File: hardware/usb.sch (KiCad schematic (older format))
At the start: 17 parts, among them J901 USB_OTG, U901 NX5P3090, U902 SMP1255PUTG, U903 USB3320, U904 OSC

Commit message: Length matched DDR3 Memory again.
Forgot to keep enough space between the traces and between the meander waves.

Also, I switched to Kicad 5.0 RC2.

Swaped a few ddr signals.
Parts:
- C901, C902, C903, C904, C905, C906, C907: symbol C -> device:C
- J901: symbol USB_OTG -> conn:USB_OTG
- R901, R902, R903, R904, R905: symbol R -> device:R
- U901: symbol NX5P3090 -> nx5p3090:NX5P3090
- U902: symbol SMP1255PUTG -> smp1255putg:SMP1255PUTG
- U903: symbol USB3320 -> usb3320:USB3320
- U904: symbol OSC -> osc:OSC
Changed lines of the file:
@@
-EESchema Schematic File Version 2
-LIBS:zynq_board-rescue
-LIBS:power
-LIBS:device
-LIBS:transistors
-LIBS:conn
-LIBS:linear
-LIBS:regul
-LIBS:74xx
-LIBS:cmos4000
-LIBS:adc-dac
-LIBS:memory
-LIBS:xilinx
-LIBS:microcontrollers
-LIBS:dsp
-LIBS:microchip
-LIBS:analog_switches
-LIBS:motorola
-LIBS:texas
-LIBS:intel
-LIBS:audio
-LIBS:interface
-LIBS:digital-audio
-LIBS:philips
-LIBS:display
-LIBS:cypress
-LIBS:siliconi
-LIBS:opto
-LIBS:atmel
-LIBS:contrib
-LIBS:valves
-LIBS:xilinx_zynq_clg485
-LIBS:SFP_plus
-LIBS:ael2005
-LIBS:diff_osc
-LIBS:si53340
-LIBS:usb3320
-LIBS:nx5p3090
-LIBS:smp1255putg
-LIBS:osc
-LIBS:ddr
-LIBS:misc
-LIBS:tlk10031
-LIBS:lshm-150-xxx-x-dv-a-s
-LIBS:sn74axc8t245
-LIBS:sn74lvc2t45
-LIBS:dmf05lcflp
-LIBS:bss138ps
-LIBS:max14854
-LIBS:switches
-LIBS:ft234xd
-LIBS:sn74lv1t126
-LIBS:emif06-msd02n16
-LIBS:cat24c02tdi-gt3
-LIBS:power_symbols
-LIBS:ti_power_modules
-LIBS:mdr20
-LIBS:dm3cs
-LIBS:lsf0102
-LIBS:dmp3056l
+EESchema Schematic File Version 4
 LIBS:zynq_board-cache
-EELAYER 25 0
+EELAYER 26 0
 EELAYER END
 $Descr A4 11693 8268
@@
 $EndDescr
 $Comp
-L USB3320 U903
+L usb3320:USB3320 U903
 U 1 1 59915033
 P 7100 3800
@@
 CLK
 $Comp
-L GND #PWR096
+L power1:GND #PWR096
 U 1 1 59921269
 P 7100 5100
@@
 NoConn ~ 6100 4700
 $Comp
-L R R905
+L device:R R905
 U 1 1 59921EA9
 P 8250 4700
@@
 $EndComp
 $Comp
-L GND #PWR097
+L power1:GND #PWR097
 U 1 1 59921EDC
 P 8500 4800
@@
 	8500 4700 8500 4800
 $Comp
-L GND #PWR098
+L power1:GND #PWR098
 U 1 1 59921F43
 P 1200 4700
@@
 $EndComp
 $Comp
-L R R901
+L device:R R901
 U 1 1 59922379
 P 1000 4550
@@
 $EndComp
 $Comp
-L GND #PWR099
+L power1:GND #PWR099
 U 1 1 599223A7
 P 1000 4700
@@
 $EndComp
 $Comp
-L R R904
+L device:R R904
 U 1 1 599227D7
 P 5750 3600
@@
 $EndComp
 $Comp
-L C C901
+L device:C C901
 U 1 1 599228B6
 P 1850 4350
@@
 	1200 4200 1200 4700
 $Comp
-L GND #PWR0100
+L power1:GND #PWR0100
 U 1 1 599229B3
 P 1850 4700
@@
 	1850 4700 1850 4500
 $Comp
-L +1V8 #PWR0101
+L power1:+1V8 #PWR0101
 U 1 1 59922E8F
 P 6850 1600
@@
 $EndComp
 $Comp
-L C C904
+L device:C C904
 U 1 1 5992426F
 P 6850 1850
@@
 $EndComp
 $Comp
-L C C905
+L device:C C905
 U 1 1 59924337
 P 7350 1850
@@
 	6850 1600 6850 1700
 $Comp
-L +1V8 #PWR0102
+L power1:+1V8 #PWR0102
 U 1 1 599243A9
 P 7350 1600
@@
 	7350 1700 7350 1600
 $Comp
-L GND #PWR0103
+L power1:GND #PWR0103
 U 1 1 5992454D
 P 7350 2000
@@
 $EndComp
 $Comp
-L GND #PWR0104
+L power1:GND #PWR0104
 U 1 1 5992459D
 P 6850 2000
@@
 Connection ~ 6850 1650
 $Comp
-L C C903
+L device:C C903
 U 1 1 59924B0A
 P 6400 1850
@@
 	6850 1650 7100 1650
 $Comp
-L +3V3 #PWR0105
+L power1:+3V3 #PWR0105
 U 1 1 59924C11
 P 6400 1600
@@
 $EndComp
 $Comp
-L GND #PWR0106
+L power1:GND #PWR0106
 U 1 1 59924C37
 P 6400 2000
@@
 VBUS overvoltage protection resistor\nPower rating for 30V protection: 0.625W
 $Comp
-L NX5P3090 U901
+L nx5p3090:NX5P3090 U901
 U 1 1 5A971EC5
 P 3800 3200
@@
 $EndComp
 $Comp
-L SMP1255PUTG U902
+L smp1255putg:SMP1255PUTG U902
 U 1 1 5A98470D
 P 3800 4600
@@
 Connection ~ 4700 4700
 $Comp
-L GND #PWR0107
+L power1:GND #PWR0107
 U 1 1 5A984E78
 P 4700 4800
@@
 $EndComp
 $Comp
-L GND #PWR0108
+L power1:GND #PWR0108
 U 1 1 5A985319
 P 3100 3400
@@
 	5350 3500 6100 3500
 $Comp
-L C C902
+L device:C C902
 U 1 1 5A9853C5
 P 4700 2750
@@
 $EndComp
 $Comp
-L GND #PWR0109
+L power1:GND #PWR0109
 U 1 1 5A985418
 P 4700 2900
@@
 $EndComp
 $Comp
-L +5V #PWR0110
+L power1:+5V #PWR0110
 U 1 1 5A985450
 P 4700 2400
@@
 	4700 4600 4700 4800
 $Comp
-L R R902
+L device:R R902
 U 1 1 5A985A8D
 P 4650 3200
@@
 $EndComp
 $Comp
-L GND #PWR0111
+L power1:GND #PWR0111
 U 1 1 5A985AE5
 P 4800 3200
@@
 ILIM current limit adjustment resistor:\nR=100k for I_ocp=581 mA typ.
 $Comp
-L R R903
+L device:R R903
 U 1 1 5A986061
 P 5150 3100
@@
 Connection ~ 5150 3300
 $Comp
-L +1V8 #PWR0112
+L power1:+1V8 #PWR0112
 U 1 1 5A9861C7
 P 5150 2950
@@
 NoConn ~ 8100 4400
 $Comp
-L OSC U904
+L osc:OSC U904
 U 1 1 5A98852C
 P 9500 4050
@@
 	10100 4150 10000 4150
 $Comp
-L GND #PWR0113
+L power1:GND #PWR0113
 U 1 1 5A98862B
 P 8900 4250
@@
 	8900 4150 9000 4150
 $Comp
-L C C907
+L device:C C907
 U 1 1 5A98874B
 P 10350 4100
@@
 Connection ~ 10050 3800
 $Comp
-L +1V8 #PWR0114
+L power1:+1V8 #PWR0114
 U 1 1 5A9888CB
 P 10050 3700
@@
 $EndComp
 $Comp
-L GND #PWR0115
+L power1:GND #PWR0115
 U 1 1 5A988966
 P 10350 4250
@@
 $EndComp
 $Comp
-L GND #PWR0116
+L power1:GND #PWR0116
 U 1 1 5A988E5D
 P 6000 3300
@@
 	5900 2450 7650 2450
 $Comp
-L C C906
+L device:C C906
 U 1 1 5A9894AA
 P 7800 1850
@@
 	7800 1600 7800 1700
 $Comp
-L GND #PWR0117
+L power1:GND #PWR0117
 U 1 1 5A989692
 P 7800 2000
@@
 Oscillator: DSC6003CI2A-012.0000\n(12 MHz)
 $Comp
-L USB_OTG J901
+L conn:USB_OTG J901
 U 1 1 5ACE0B3C
 P 1200 3800
@@
 	1100 4300 1100 4200
 $Comp
-L +3V3 #PWR0118
+L power1:+3V3 #PWR0118
 U 1 1 5B1F6406
 P 7800 1600

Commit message: Layouted USB-UART.
Also moved USB-OTG to the right Side of the Board. To get there
some free Space, i moved the DDR3/Memory and the FPGA a few
Millimeters down.
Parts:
- R901, R902, R903, R904, R905: footprint Resistors_SMD:R_0402 -> Resistor_SMD:R_0402_1005Metric
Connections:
- net labels added: USB_OTG_N, USB_OTG_P
- wire segments 70 -> 88
- no-connect marks 6 -> 4
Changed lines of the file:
@@
 F 0 "R905" V 8330 4700 50  0000 C CNN
 F 1 "8.06k" V 8250 4700 50  0000 C CNN
-F 2 "Resistors_SMD:R_0402" V 8180 4700 50  0001 C CNN
+F 2 "Resistor_SMD:R_0402_1005Metric" V 8180 4700 50  0001 C CNN
 F 3 "" H 8250 4700 50  0000 C CNN
 	1    8250 4700
@@
 F 0 "R901" V 1080 4550 50  0000 C CNN
 F 1 "0" V 1000 4550 50  0000 C CNN
-F 2 "Resistors_SMD:R_0402" V 930 4550 50  0001 C CNN
+F 2 "Resistor_SMD:R_0402_1005Metric" V 930 4550 50  0001 C CNN
 F 3 "" H 1000 4550 50  0000 C CNN
 	1    1000 4550
@@
 F 0 "R904" V 5830 3600 50  0000 C CNN
 F 1 "1k" V 5750 3600 50  0000 C CNN
-F 2 "Resistors_SMD:R_0402" V 5680 3600 50  0001 C CNN
+F 2 "Resistor_SMD:R_0402_1005Metric" V 5680 3600 50  0001 C CNN
 F 3 "" H 5750 3600 50  0000 C CNN
 	1    5750 3600
@@
 $EndComp
 Wire Wire Line
-	6850 1600 6850 1700
+	6850 1600 6850 1650
 $Comp
 L power1:+1V8 #PWR0102
@@
 $EndComp
 Wire Wire Line
-	7350 1700 7350 1600
+	7350 1700 7350 1650
 $Comp
 L power1:GND #PWR0103
@@
 $EndComp
 Wire Wire Line
-	6400 1600 6400 1700
+	6400 1600 6400 1650
 Wire Wire Line
 	6900 2500 6900 2350
 Wire Wire Line
-	6900 2350 6650 2350
+	6900 2350 6750 2350
 Wire Wire Line
 	6650 2350 6650 1650
@@
 $EndComp
 Wire Wire Line
-	3000 4500 2900 4500
-Wire Wire Line
-	3000 4600 2800 4600
-Wire Wire Line
 	3000 4700 2700 4700
 Wire Wire Line
@@
 $EndComp
 Wire Wire Line
-	4700 2400 4700 2600
+	4700 2400 4700 2500
 Wire Wire Line
 	4500 3000 4500 2500
@@
 Connection ~ 4700 2500
 Wire Wire Line
-	4700 4600 4700 4800
+	4700 4600 4700 4700
 $Comp
 L device:R R902
@@
 F 0 "R902" V 4730 3200 50  0000 C CNN
 F 1 "100k" V 4650 3200 50  0000 C CNN
-F 2 "Resistors_SMD:R_0402" V 4580 3200 50  0001 C CNN
+F 2 "Resistor_SMD:R_0402_1005Metric" V 4580 3200 50  0001 C CNN
 F 3 "" H 4650 3200 50  0000 C CNN
 	1    4650 3200
@@
 F 0 "R903" V 5230 3100 50  0000 C CNN
 F 1 "10k" V 5150 3100 50  0000 C CNN
-F 2 "Resistors_SMD:R_0402" V 5080 3100 50  0001 C CNN
+F 2 "Resistor_SMD:R_0402_1005Metric" V 5080 3100 50  0001 C CNN
 F 3 "" H 5150 3100 50  0000 C CNN
 	1    5150 3100
@@
 VBUS_FAULT
 Wire Wire Line
-	4500 3300 5250 3300
+	4500 3300 5150 3300
 Wire Wire Line
 	5150 3300 5150 3250
@@
 	9000 3950 9000 3800
 Wire Wire Line
-	9000 3800 10350 3800
+	9000 3800 10050 3800
 Wire Wire Line
 	10350 3800 10350 3950
@@
 	10050 3950 10000 3950
 Wire Wire Line
-	10050 3700 10050 3950
+	10050 3700 10050 3800
 Connection ~ 10050 3800
 $Comp
@@
 $EndComp
 Wire Wire Line
-	6000 3300 6000 3000
+	6000 3300 6000 3200
 Wire Wire Line
 	6000 3000 6100 3000
@@
 	5900 2450 5900 3100
 Wire Wire Line
-	5900 2450 7650 2450
+	5900 2450 7400 2450
 $Comp
 L device:C C906
@@
 	7650 1650 7800 1650
 Wire Wire Line
-	7800 1600 7800 1700
+	7800 1600 7800 1650
 $Comp
 L power1:GND #PWR0117
@@
 $EndComp
 Wire Wire Line
-	1500 3600 5600 3600
+	1500 3600 1850 3600
 Wire Wire Line
 	6100 4000 5950 4000
@@
 	5950 4000 5950 3800
 Wire Wire Line
-	5950 3800 1500 3800
-Wire Wire Line
-	6100 3900 1500 3900
-Wire Wire Line
-	1500 4000 5850 4000
+	5950 3800 2900 3800
+Wire Wire Line
+	6100 3900 2800 3900
+Wire Wire Line
+	1500 4000 2700 4000
 Wire Wire Line
 	5850 4000 5850 4100
 Wire Wire Line
 	5850 4100 6100 4100
-Wire Wire Line
-	2900 4500 2900 3800
 Connection ~ 2900 3800
 Wire Wire Line
-	2800 4600 2800 3900
+	2800 4500 2800 3900
 Connection ~ 2800 3900
 Wire Wire Line
@@
 	1    0    0    -1
 $EndComp
-NoConn ~ 4000 4700
 NoConn ~ 3950 3300
-NoConn ~ 3900 4700
 Text Notes 700  3000 0    60   ~ 0
 TODO: correct MicroUSB Footprint
+Wire Wire Line
+	1850 3600 2700 3600
+Wire Wire Line
+	7350 1650 7350 1600
+Wire Wire Line
+	6850 1650 6850 1700
+Wire Wire Line
+	6400 1650 6400 1700
+Wire Wire Line
+	6750 2350 6650 2350
+Wire Wire Line
+	2700 3600 4700 3600
+Wire Wire Line
+	4700 3600 5600 3600
+Wire Wire Line
+	4700 4700 4700 4800
+Wire Wire Line
+	4700 2500 4700 2600
+Wire Wire Line
+	5150 3300 5250 3300
+Wire Wire Line
+	10050 3800 10350 3800
+Wire Wire Line
+	10050 3800 10050 3950
+Wire Wire Line
+	6000 3200 6000 3000
+Wire Wire Line
+	7400 2450 7650 2450
+Wire Wire Line
+	7800 1650 7800 1700
+Wire Wire Line
+	2900 3800 1500 3800
+Wire Wire Line
+	2800 3900 1500 3900
+Wire Wire Line
+	2700 4000 5850 4000
+Text Label 3250 3800 0    50   ~ 0
+USB_OTG_P
+Text Label 3250 3900 0    50   ~ 0
+USB_OTG_N
+Wire Wire Line
+	2900 4600 3000 4600
+Wire Wire Line
+	2900 3800 2900 4600
+Wire Wire Line
+	2800 4500 3000 4500
 $EndSCHEMATC

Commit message: Improved Powerdistribution Network of the FPGA.
Also started to layout USB.
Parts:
- removed C901, C903: 2u2, Capacitors_SMD:C_0402, symbol device:C
- removed C902, C904, C905, C906, C907: 100n, Capacitors_SMD:C_0402, symbol device:C
- added C901: 2,2 µF, Capacitor_SMD:C_0603_1608Metric, symbol Device:C_Small
- added C902, C903, C904, C905, C906, C907: 100 nF, Capacitor_SMD:C_0201_0603Metric, symbol device:C_Small
- U904: footprint footprints:VDFN_3.2x2.5mm -> footprints:Microchip_CDFN_3.2x2.5mm; Populate for CLG484(Z-7012s/Z-7015) (none) -> 1; Populate for SBGA485(Z-7030) (none) -> 1
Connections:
- wire segments 88 -> 94
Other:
- note added: "Bypass Cap for external\n3,3 V Supply is only C_BYP\nwith 100 nF"

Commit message: Fixed Schematic Symbols
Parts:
- C902, C903, C904, C905, C906, C907: symbol device:C_Small -> Device:C_Small
- J901: symbol conn:USB_OTG -> Connector:USB_OTG
- R901, R902, R903, R904, R905: symbol device:R -> Device:R
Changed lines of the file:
@@
 $Descr A4 11693 8268
 encoding utf-8
-Sheet 9 22
+Sheet 8 21
 Title ""
 Date ""
@@
 CLK
 $Comp
-L power1:GND #PWR096
+L power:GND #PWR096
 U 1 1 59921269
 P 7100 5100
@@
 NoConn ~ 6100 4700
 $Comp
-L device:R R905
+L Device:R R905
 U 1 1 59921EA9
 P 8250 4700
@@
 $EndComp
 $Comp
-L power1:GND #PWR097
+L power:GND #PWR097
 U 1 1 59921EDC
 P 8500 4800
@@
 	8500 4700 8500 4800
 $Comp
-L power1:GND #PWR098
+L power:GND #PWR098
 U 1 1 59921F43
 P 1200 4700
@@
 $EndComp
 $Comp
-L device:R R901
+L Device:R R901
 U 1 1 59922379
 P 1000 4550
@@
 $EndComp
 $Comp
-L power1:GND #PWR099
+L power:GND #PWR099
 U 1 1 599223A7
 P 1000 4700
@@
 $EndComp
 $Comp
-L device:R R904
+L Device:R R904
 U 1 1 599227D7
 P 5750 3600
@@
 	1200 4200 1200 4700
 $Comp
-L power1:GND #PWR0100
+L power:GND #PWR0100
 U 1 1 599229B3
 P 1850 4700
@@
 $EndComp
 $Comp
-L power1:+1V8 #PWR0101
+L power:+1V8 #PWR0101
 U 1 1 59922E8F
 P 6850 1600
@@
 	6850 1600 6850 1650
 $Comp
-L power1:+1V8 #PWR0102
+L power:+1V8 #PWR0102
 U 1 1 599243A9
 P 7350 1600
@@
 $EndComp
 $Comp
-L power1:GND #PWR0103
+L power:GND #PWR0103
 U 1 1 5992454D
 P 7350 2000
@@
 $EndComp
 $Comp
-L power1:GND #PWR0104
+L power:GND #PWR0104
 U 1 1 5992459D
 P 6850 2000
@@
 	6850 1650 7100 1650
 $Comp
-L power1:+3V3 #PWR0105
+L power:+3V3 #PWR0105
 U 1 1 59924C11
 P 6400 1600
@@
 $EndComp
 $Comp
-L power1:GND #PWR0106
+L power:GND #PWR0106
 U 1 1 59924C37
 P 6400 2000
@@
 Connection ~ 4700 4700
 $Comp
-L power1:GND #PWR0107
+L power:GND #PWR0107
 U 1 1 5A984E78
 P 4700 4800
@@
 $EndComp
 $Comp
-L power1:GND #PWR0108
+L power:GND #PWR0108
 U 1 1 5A985319
 P 3100 3400
@@
 	5350 3500 6100 3500
 $Comp
-L power1:GND #PWR0109
+L power:GND #PWR0109
 U 1 1 5A985418
 P 4700 2900
@@
 $EndComp
 $Comp
-L power1:+5V #PWR0110
+L power:+5V #PWR0110
 U 1 1 5A985450
 P 4700 2400
@@
 	4700 4600 4700 4700
 $Comp
-L device:R R902
+L Device:R R902
 U 1 1 5A985A8D
 P 4650 3200
@@
 $EndComp
 $Comp
-L power1:GND #PWR0111
+L power:GND #PWR0111
 U 1 1 5A985AE5
 P 4800 3200
@@
 ILIM current limit adjustment resistor:\nR=100k for I_ocp=581 mA typ.
 $Comp
-L device:R R903
+L Device:R R903
 U 1 1 5A986061
 P 5150 3100
@@
 Connection ~ 5150 3300
 $Comp
-L power1:+1V8 #PWR0112
+L power:+1V8 #PWR0112
 U 1 1 5A9861C7
 P 5150 2950
@@
 	10100 4150 10000 4150
 $Comp
-L power1:GND #PWR0113
+L power:GND #PWR0113
 U 1 1 5A98862B
 P 8900 4250
@@
 Connection ~ 10050 3800
 $Comp
-L power1:+1V8 #PWR0114
+L power:+1V8 #PWR0114
 U 1 1 5A9888CB
 P 10050 3700
@@
 $EndComp
 $Comp
-L power1:GND #PWR0115
+L power:GND #PWR0115
 U 1 1 5A988966
 P 10350 4250
@@
 $EndComp
 $Comp
-L power1:GND #PWR0116
+L power:GND #PWR0116
 U 1 1 5A988E5D
 P 6000 3300
@@
 	7800 1600 7800 1650
 $Comp
-L power1:GND #PWR0117
+L power:GND #PWR0117
 U 1 1 5A989692
 P 7800 2000
@@
 Oscillator: DSC6003CI2A-012.0000\n(12 MHz)
 $Comp
-L conn:USB_OTG J901
+L Connector:USB_OTG J901
 U 1 1 5ACE0B3C
 P 1200 3800
@@
 	1100 4300 1100 4200
 $Comp
-L power1:+3V3 #PWR0118
+L power:+3V3 #PWR0118
 U 1 1 5B1F6406
 P 7800 1600
@@
 	2800 4500 3000 4500
 $Comp
-L device:C_Small C904
+L Device:C_Small C904
 U 1 1 5B2225E7
 P 6850 1850
@@
 $EndComp
 $Comp
-L device:C_Small C905
+L Device:C_Small C905
 U 1 1 5B224CCE
 P 7350 1850
@@
 $EndComp
 $Comp
-L device:C_Small C906
+L Device:C_Small C906
 U 1 1 5B224D20
 P 7800 1850
@@
 $EndComp
 $Comp
-L device:C_Small C907
+L Device:C_Small C907
 U 1 1 5B224D9D
 P 10350 4100
@@
 $EndComp
 $Comp
-L device:C_Small C902
+L Device:C_Small C902
 U 1 1 5B224E9D
 P 4700 2750
@@
 	10350 3800 10350 4000
 $Comp
-L device:C_Small C903
+L Device:C_Small C903
 U 1 1 5B23D5EF
 P 6400 1850

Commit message: WIP: TLK Powerdistribution
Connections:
- no-connect marks 4 -> 3
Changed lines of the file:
@@
 EESchema Schematic File Version 4
-LIBS:zynq_board-cache
 EELAYER 26 0
 EELAYER END
@@
 	1    0    0    -1
 $EndComp
-NoConn ~ 3950 3300
 Text Notes 700  3000 0    60   ~ 0
 TODO: correct MicroUSB Footprint

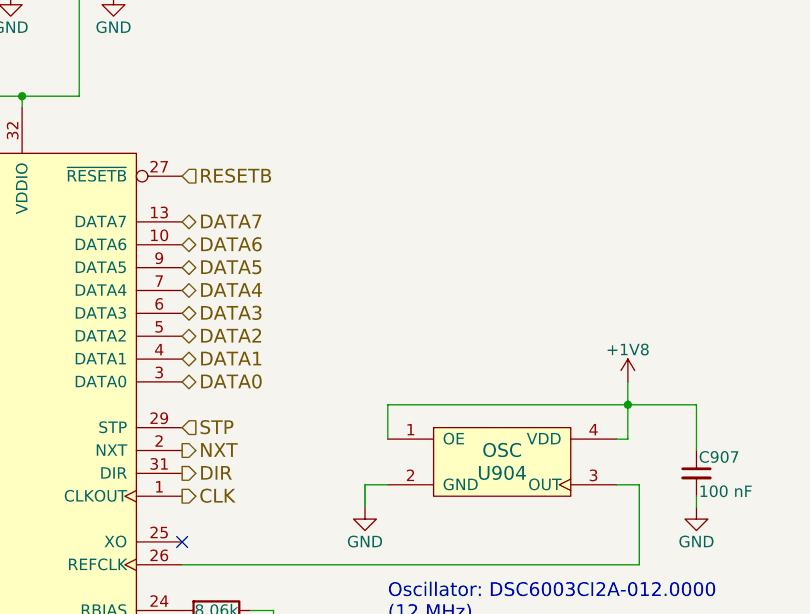
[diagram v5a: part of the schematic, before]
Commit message: WIP: routing the HF Part of the Camera Connector. I have to move the clock away from the left border.
TODO: Fix DDR3 RAM.
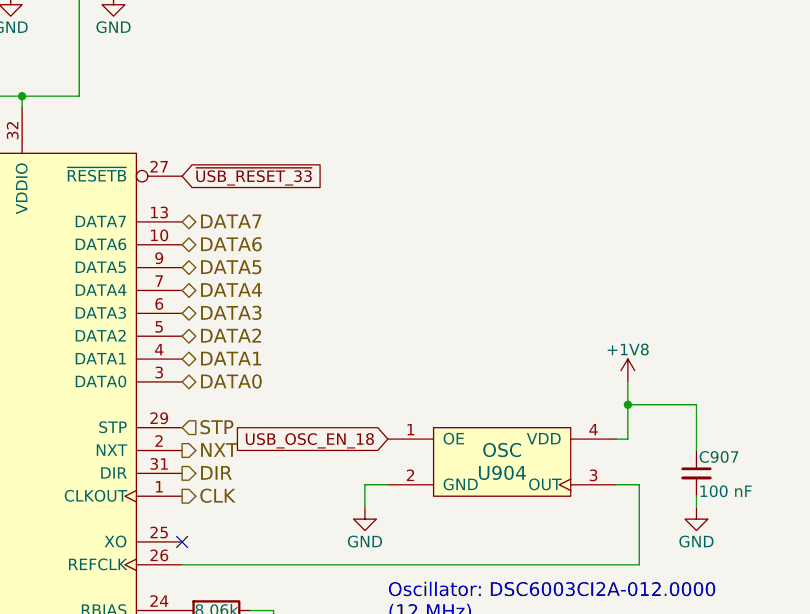
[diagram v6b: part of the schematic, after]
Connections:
- net +1V8: no longer U904.1 (OE)
- net RESETB renamed ~USB_RESET_33~
- new net USB_OSC_EN_18: U904.1 (OE)
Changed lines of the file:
@@
 $EndComp
 NoConn ~ 8100 4400
-$Comp
-L osc:OSC U904
-U 1 1 5A98852C
-P 9500 4050
-F 0 "U904" H 9500 4000 60  0000 C CNN
-F 1 "OSC" H 9500 4100 60  0000 C CNN
-F 2 "footprints:Microchip_CDFN_3.2x2.5mm" H 9500 4050 60  0001 C CNN
-F 3 "http://www.microchip.com/mymicrochip/filehandler.aspx?ddocname=en587489" H 9500 4050 60  0001 C CNN
-F 4 "Microchip Technology" H 9500 4050 60  0001 C CNN "MFG Name"
-F 5 "DSC6003CI2A-012.0000" H 9500 4050 60  0001 C CNN "MFG Part Num"
-F 6 "DSC6003CI2A-012.0000-ND" H 9500 4050 60  0001 C CNN "Digikey"
-F 7 "579-C6003CI2A0120000" H 9500 4050 60  0001 C CNN "Mouser"
-F 8 "1" H 9500 4050 60  0001 C CNN "Populated"
-F 9 "SPEC" H 9500 4050 60  0001 C CNN "Source"
-F 10 "1" H 9500 4050 50  0001 C CNN "Populate for SBGA485(Z-7030)"
-F 11 "1" H 9500 4050 50  0001 C CNN "Populate for CLG484(Z-7012s/Z-7015)"
-	1    9500 4050
-	1    0    0    -1
-$EndComp
 Wire Wire Line
 	8100 4500 10100 4500
@@
 	8900 4150 9000 4150
 Wire Wire Line
-	9000 3950 9000 3800
-Wire Wire Line
-	9000 3800 10050 3800
-Wire Wire Line
 	10050 3950 10000 3950
 Wire Wire Line
@@
 Text Notes 5150 2400 0    60   ~ 0
 REFSEL[2:0] = 010\nto select 12 MHz\nREFCLK input
-Text HLabel 8100 2800 2    60   Input ~ 0
-RESETB
 Text Notes 9000 4750 0    60   ~ 0
 Oscillator: DSC6003CI2A-012.0000\n(12 MHz)
@@
 Text Notes 5300 1850 0    50   ~ 0
 Bypass Cap for external\n3,3 V Supply is only C_BYP\nwith 100 nF
+Text GLabel 8100 2800 2    50   Input ~ 0
+~USB_RESET_33~
+$Comp
+L osc:OSC U904
+U 1 1 5A98852C
+P 9500 4050
+F 0 "U904" H 9500 4000 60  0000 C CNN
+F 1 "OSC" H 9500 4100 60  0000 C CNN
+F 2 "footprints:Microchip_CDFN_3.2x2.5mm" H 9500 4050 60  0001 C CNN
+F 3 "http://www.microchip.com/mymicrochip/filehandler.aspx?ddocname=en587489" H 9500 4050 60  0001 C CNN
+F 4 "Microchip Technology" H 9500 4050 60  0001 C CNN "MFG Name"
+F 5 "DSC6003CI2A-012.0000" H 9500 4050 60  0001 C CNN "MFG Part Num"
+F 6 "DSC6003CI2A-012.0000-ND" H 9500 4050 60  0001 C CNN "Digikey"
+F 7 "579-C6003CI2A0120000" H 9500 4050 60  0001 C CNN "Mouser"
+F 8 "1" H 9500 4050 60  0001 C CNN "Populated"
+F 9 "SPEC" H 9500 4050 60  0001 C CNN "Source"
+F 10 "1" H 9500 4050 50  0001 C CNN "Populate for SBGA485(Z-7030)"
+F 11 "1" H 9500 4050 50  0001 C CNN "Populate for CLG484(Z-7012s/Z-7015)"
+	1    9500 4050
+	1    0    0    -1
+$EndComp
+Text GLabel 9000 3950 0    50   Input ~ 0
+USB_OSC_EN_18
 $EndSCHEMATC
